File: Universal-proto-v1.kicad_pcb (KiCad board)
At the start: 2 copper layers, 2 parts, among them J1 Bus_ISA_8bit, U1 RP2350B

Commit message: Start work on PCB
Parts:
- added J2: ISA Breakout, Connector_PinHeader_2.54mm:PinHeader_2x31_P2.54mm_Vertical, F.Cu at (185.8, 127.5)
- added J3: Pico GPIO Breakout, Connector_PinHeader_2.54mm:PinHeader_2x25_P2.54mm_Vertical, F.Cu at (180.5, 75.0)
- added JP1: SolderJumper_2_Bridged, Jumper:SolderJumper-2_P1.3mm_Bridged_RoundedPad1.0x1.5mm, F.Cu at (109.5, 122.0)
- added JP10: SolderJumper_2_Bridged, Jumper:SolderJumper-2_P1.3mm_Bridged_RoundedPad1.0x1.5mm, F.Cu at (132.4, 122.0)
- added JP11: SolderJumper_2_Bridged, Jumper:SolderJumper-2_P1.3mm_Bridged_RoundedPad1.0x1.5mm, F.Cu at (134.9, 122.0)
- added JP12: SolderJumper_2_Bridged, Jumper:SolderJumper-2_P1.3mm_Bridged_RoundedPad1.0x1.5mm, F.Cu at (137.5, 122.0)
- added JP13: SolderJumper_2_Bridged, Jumper:SolderJumper-2_P1.3mm_Bridged_RoundedPad1.0x1.5mm, F.Cu at (140.0, 122.0)
- added JP14: SolderJumper_2_Bridged, Jumper:SolderJumper-2_P1.3mm_Bridged_RoundedPad1.0x1.5mm, F.Cu at (142.6, 122.0)
- added JP15: SolderJumper_2_Bridged, Jumper:SolderJumper-2_P1.3mm_Bridged_RoundedPad1.0x1.5mm, F.Cu at (145.1, 122.0)
- added JP16: SolderJumper_2_Bridged, Jumper:SolderJumper-2_P1.3mm_Bridged_RoundedPad1.0x1.5mm, F.Cu at (147.6, 122.0)
- added JP17: SolderJumper_2_Bridged, Jumper:SolderJumper-2_P1.3mm_Bridged_RoundedPad1.0x1.5mm, F.Cu at (150.2, 122.0)
- added JP18: SolderJumper_2_Bridged, Jumper:SolderJumper-2_P1.3mm_Bridged_RoundedPad1.0x1.5mm, F.Cu at (152.7, 122.0)
- added JP19: SolderJumper_2_Bridged, Jumper:SolderJumper-2_P1.3mm_Bridged_RoundedPad1.0x1.5mm, F.Cu at (155.3, 122.0)
- added JP2: SolderJumper_2_Bridged, Jumper:SolderJumper-2_P1.3mm_Bridged_RoundedPad1.0x1.5mm, F.Cu at (112.0, 122.0)
- added JP20: SolderJumper_2_Bridged, Jumper:SolderJumper-2_P1.3mm_Bridged_RoundedPad1.0x1.5mm, F.Cu at (157.8, 122.0)
- added JP21: SolderJumper_2_Bridged, Jumper:SolderJumper-2_P1.3mm_Bridged_RoundedPad1.0x1.5mm, F.Cu at (165.4, 122.0)
- added JP22: SolderJumper_2_Bridged, Jumper:SolderJumper-2_P1.3mm_Bridged_RoundedPad1.0x1.5mm, F.Cu at (168.0, 122.0)
- added JP23: SolderJumper_2_Bridged, Jumper:SolderJumper-2_P1.3mm_Bridged_RoundedPad1.0x1.5mm, F.Cu at (170.5, 122.0)
- added JP24: SolderJumper_2_Bridged, Jumper:SolderJumper-2_P1.3mm_Bridged_RoundedPad1.0x1.5mm, F.Cu at (173.1, 122.0)
- added JP25: SolderJumper_2_Bridged, Jumper:SolderJumper-2_P1.3mm_Bridged_RoundedPad1.0x1.5mm, F.Cu at (175.6, 122.0)
- added JP26: SolderJumper_2_Bridged, Jumper:SolderJumper-2_P1.3mm_Bridged_RoundedPad1.0x1.5mm, F.Cu at (178.1, 122.0)
- added JP27: SolderJumper_2_Bridged, Jumper:SolderJumper-2_P1.3mm_Bridged_RoundedPad1.0x1.5mm, F.Cu at (180.7, 122.0)
- added JP28: SolderJumper_2_Bridged, Jumper:SolderJumper-2_P1.3mm_Bridged_RoundedPad1.0x1.5mm, F.Cu at (183.2, 122.0)
- added JP29: SolderJumper_2_Bridged, Jumper:SolderJumper-2_P1.3mm_Bridged_RoundedPad1.0x1.5mm, B.Cu at (157.8, 122.0)
- added JP3: SolderJumper_2_Bridged, Jumper:SolderJumper-2_P1.3mm_Bridged_RoundedPad1.0x1.5mm, F.Cu at (114.6, 122.0)
- added JP30: SolderJumper_2_Bridged, Jumper:SolderJumper-2_P1.3mm_Bridged_RoundedPad1.0x1.5mm, B.Cu at (160.4, 122.0)
- added JP31: SolderJumper_2_Bridged, Jumper:SolderJumper-2_P1.3mm_Bridged_RoundedPad1.0x1.5mm, B.Cu at (152.7, 122.0)
- added JP32: SolderJumper_2_Bridged, Jumper:SolderJumper-2_P1.3mm_Bridged_RoundedPad1.0x1.5mm, B.Cu at (155.3, 122.0)
- added JP33: SolderJumper_2_Bridged, Jumper:SolderJumper-2_P1.3mm_Bridged_RoundedPad1.0x1.5mm, F.Cu at (160.4, 122.0)
- added JP34: SolderJumper_2_Bridged, Jumper:SolderJumper-2_P1.3mm_Bridged_RoundedPad1.0x1.5mm, B.Cu at (137.5, 122.0)
- added JP35: SolderJumper_2_Bridged, Jumper:SolderJumper-2_P1.3mm_Bridged_RoundedPad1.0x1.5mm, B.Cu at (117.2, 122.0)
- added JP36: SolderJumper_2_Bridged, Jumper:SolderJumper-2_P1.3mm_Bridged_RoundedPad1.0x1.5mm, B.Cu at (183.2, 122.0)
- added JP37: SolderJumper_2_Open, Jumper:SolderJumper-2_P1.3mm_Open_Pad1.0x1.5mm, B.Cu at (165.5, 133.8)
- added JP38: SolderJumper_2_Open, Jumper:SolderJumper-2_P1.3mm_Open_Pad1.0x1.5mm, B.Cu at (170.6, 133.8)
- added JP39: SolderJumper_2_Open, Jumper:SolderJumper-2_P1.3mm_Open_Pad1.0x1.5mm, B.Cu at (175.7, 133.8)
- added JP4: SolderJumper_2_Bridged, Jumper:SolderJumper-2_P1.3mm_Bridged_RoundedPad1.0x1.5mm, F.Cu at (117.1, 122.0)
- added JP5: SolderJumper_2_Bridged, Jumper:SolderJumper-2_P1.3mm_Bridged_RoundedPad1.0x1.5mm, F.Cu at (119.7, 122.0)
- added JP6: SolderJumper_2_Bridged, Jumper:SolderJumper-2_P1.3mm_Bridged_RoundedPad1.0x1.5mm, F.Cu at (122.2, 122.0)
- added JP7: SolderJumper_2_Bridged, Jumper:SolderJumper-2_P1.3mm_Bridged_RoundedPad1.0x1.5mm, F.Cu at (124.8, 122.0)
- added JP8: SolderJumper_2_Bridged, Jumper:SolderJumper-2_P1.3mm_Bridged_RoundedPad1.0x1.5mm, F.Cu at (127.3, 122.0)
- added JP9: SolderJumper_2_Bridged, Jumper:SolderJumper-2_P1.3mm_Bridged_RoundedPad1.0x1.5mm, F.Cu at (129.8, 122.0)
- added U2: ~, FujiNet:ESP32-S3-CAM, F.Cu at (183.5, 40.8)
- U1: value RP2350B -> ~; footprint Package_DFN_QFN:QFN-80-1EP_10x10mm_P0.4mm_EP3.4x3.4mm -> FujiNet:WaveShare-Core-RP2350B
- moved J1 78.6 mm to (185.9, 140.0)
- moved U1 35.5 mm to (90.9, 71.9)
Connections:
- J1 pad 1: unconnected-(J1-GND-Pad1) -> /GND
- J1 pad 10: unconnected-(J1-GND-Pad10) -> /GND
- J1 pad 11: unconnected-(J1-~{SMEMW}-Pad11) -> /~{SMEMW}
- J1 pad 12: unconnected-(J1-~{SMEMR}-Pad12) -> /~{SMEMR}
- J1 pad 13: unconnected-(J1-~{IOW}-Pad13) -> /~{IOW}
- J1 pad 14: unconnected-(J1-~{IOR}-Pad14) -> /~{IOR}
- J1 pad 15: unconnected-(J1-~{DACK3}-Pad15) -> /~{DACK3}
- J1 pad 16: unconnected-(J1-DRQ3-Pad16) -> /DRQ3
- J1 pad 17: unconnected-(J1-~{DACK1}-Pad17) -> /~{DACK1}
- J1 pad 18: unconnected-(J1-DRQ1-Pad18) -> /DRQ1
- J1 pad 19: unconnected-(J1-~{DACK0}-Pad19) -> /~{DACK0}
- J1 pad 2: unconnected-(J1-RESET-Pad2) -> /RESET
- J1 pad 20: unconnected-(J1-CLK-Pad20) -> /CLK
- J1 pad 21: unconnected-(J1-IRQ7-Pad21) -> /IRQ7
- J1 pad 22: unconnected-(J1-IRQ6-Pad22) -> /IRQ6
- J1 pad 23: unconnected-(J1-IRQ5-Pad23) -> /IRQ5
- J1 pad 24: unconnected-(J1-IRQ4-Pad24) -> /IRQ4
- J1 pad 25: unconnected-(J1-IRQ3-Pad25) -> /IRQ3
- J1 pad 26: unconnected-(J1-~{DACK2}-Pad26) -> /~{DACK2}
- J1 pad 27: unconnected-(J1-TC-Pad27) -> /TC
- J1 pad 28: unconnected-(J1-ALE-Pad28) -> /ALE
- J1 pad 29: unconnected-(J1-VCC-Pad29) -> /VCC
- J1 pad 3: unconnected-(J1-VCC-Pad3) -> /VCC
- J1 pad 30: unconnected-(J1-OSC-Pad30) -> /OSC
- J1 pad 31: unconnected-(J1-GND-Pad31) -> /GND
- J1 pad 32: unconnected-(J1-IO-Pad32) -> /IO
- J1 pad 33: unconnected-(J1-DB7-Pad33) -> /DB7
- J1 pad 34: unconnected-(J1-DB6-Pad34) -> /DB6
- J1 pad 35: unconnected-(J1-DB5-Pad35) -> /DB5
- J1 pad 36: unconnected-(J1-DB4-Pad36) -> /DB4
- J1 pad 37: unconnected-(J1-DB3-Pad37) -> /DB3
- J1 pad 38: unconnected-(J1-DB2-Pad38) -> /DB2
- J1 pad 39: unconnected-(J1-DB1-Pad39) -> /DB1
- J1 pad 4: unconnected-(J1-IRQ2-Pad4) -> /IRQ2
- J1 pad 40: unconnected-(J1-DB0-Pad40) -> /DB0
- J1 pad 41: unconnected-(J1-IO_READY-Pad41) -> /IO_READY
- J1 pad 42: unconnected-(J1-AEN-Pad42) -> /AEN
- J1 pad 43: unconnected-(J1-BA19-Pad43) -> /BA19
- J1 pad 44: unconnected-(J1-BA18-Pad44) -> /BA18
- J1 pad 45: unconnected-(J1-BA17-Pad45) -> /BA17
- J1 pad 46: unconnected-(J1-BA16-Pad46) -> /BA16
- J1 pad 47: unconnected-(J1-BA15-Pad47) -> /BA15
- J1 pad 48: unconnected-(J1-BA14-Pad48) -> /BA14
- J1 pad 49: unconnected-(J1-BA13-Pad49) -> /BA13
- J1 pad 5: unconnected-(J1--5V-Pad5) -> /ISA_-5V
- J1 pad 50: unconnected-(J1-BA12-Pad50) -> /BA12
- J1 pad 51: unconnected-(J1-BA11-Pad51) -> /BA11
- J1 pad 52: unconnected-(J1-BA10-Pad52) -> /BA10
- J1 pad 53: unconnected-(J1-BA09-Pad53) -> /BA09
- J1 pad 54: unconnected-(J1-BA08-Pad54) -> /BA08
- J1 pad 55: unconnected-(J1-BA07-Pad55) -> /BA07
- J1 pad 56: unconnected-(J1-BA06-Pad56) -> /BA06
- J1 pad 57: unconnected-(J1-BA05-Pad57) -> /BA05
- J1 pad 58: unconnected-(J1-BA04-Pad58) -> /BA04
- J1 pad 59: unconnected-(J1-BA03-Pad59) -> /BA03
- J1 pad 6: unconnected-(J1-DRQ2-Pad6) -> /DRQ2
- J1 pad 60: unconnected-(J1-BA02-Pad60) -> /BA02
- J1 pad 61: unconnected-(J1-BA01-Pad61) -> /BA01
- J1 pad 62: unconnected-(J1-BA00-Pad62) -> /BA00
- J1 pad 7: unconnected-(J1--12V-Pad7) -> /ISA_-12V
- J1 pad 8: unconnected-(J1-UNUSED-Pad8) -> /UNUSED
- J1 pad 9: unconnected-(J1-+12V-Pad9) -> /ISA_+12V
- U1 pad 1: unconnected-(U1-GPIO4-Pad1) -> /GP1_ISA_A1
- U1 pad 10: Net-(U1-DVDD-Pad10) -> /GP10_ISA_A10
- U1 pad 11: unconnected-(U1-GPIO12-Pad11) -> /GP11_ISA_A11
- U1 pad 12: unconnected-(U1-GPIO13-Pad12) -> /GP12_ISA_A12
- U1 pad 13: unconnected-(U1-GPIO14-Pad13) -> /GP13_ISA_A13
- U1 pad 14: unconnected-(U1-GPIO15-Pad14) -> /GP14_ISA_A14
- U1 pad 15: Net-(U1-IOVDD-Pad15) -> /GP15_ISA_A15
- U1 pad 16: unconnected-(U1-GPIO16-Pad16) -> /GP16_ISA_A16
- U1 pad 17: unconnected-(U1-GPIO17-Pad17) -> /GP17_ISA_A17
- U1 pad 18: unconnected-(U1-GPIO18-Pad18) -> /GP18_ISA_A18
- U1 pad 19: unconnected-(U1-GPIO19-Pad19) -> /GP19_ISA_A19
- U1 pad 2: unconnected-(U1-GPIO5-Pad2) -> /GP2_ISA_A2
- U1 pad 20: unconnected-(U1-GPIO20-Pad20) -> /GP20_ISA_D0
- U1 pad 21: unconnected-(U1-GPIO21-Pad21) -> /GP21_ISA_D1
- U1 pad 22: unconnected-(U1-GPIO22-Pad22) -> /GP22_ISA_D2
- U1 pad 23: unconnected-(U1-GPIO23-Pad23) -> /GP23_ISA_D3
- U1 pad 24: Net-(U1-IOVDD-Pad15) -> /GP24_ISA_D4
- U1 pad 25: unconnected-(U1-GPIO24-Pad25) -> /GP25_ISA_D5
- U1 pad 26: unconnected-(U1-GPIO25-Pad26) -> /GP26_ISA_D6
- U1 pad 27: unconnected-(U1-GPIO26-Pad27) -> /GP27_ISA_D7
- U1 pad 28: unconnected-(U1-GPIO27-Pad28) -> /GP28_ISA_MEMR
- U1 pad 29: Net-(U1-IOVDD-Pad15) -> /GP29_ISA_MEMW
- U1 pad 3: unconnected-(U1-GPIO6-Pad3) -> /GP3_ISA_A3
- U1 pad 30: unconnected-(U1-XIN-Pad30) -> /GP30_ISA_IOR
- U1 pad 31: unconnected-(U1-XOUT-Pad31) -> /GP31_ISA_IOW
- U1 pad 32: Net-(U1-DVDD-Pad10) -> /GP32_ISA_AEN
- U1 pad 33: unconnected-(U1-SWCLK-Pad33) -> /GP33_ISA_CLK
- U1 pad 34: unconnected-(U1-SWDIO-Pad34) -> /GP34_ISA_ALE
- U1 pad 35: unconnected-(U1-RUN-Pad35) -> /GP35_ISA_RESET
- U1 pad 36: unconnected-(U1-GPIO28-Pad36) -> /GP36
- U1 pad 37: unconnected-(U1-GPIO29-Pad37) -> /GP37
- U1 pad 38: unconnected-(U1-GPIO30-Pad38) -> /GP38
- U1 pad 39: unconnected-(U1-GPIO31-Pad39) -> /GP39
- U1 pad 4: unconnected-(U1-GPIO7-Pad4) -> /GP4_ISA_A4
- U1 pad 40: unconnected-(U1-GPIO32-Pad40) -> /GP40
- U1 pad 41: Net-(U1-IOVDD-Pad15) -> /GP41
- U1 pad 42: unconnected-(U1-GPIO33-Pad42) -> /GP42
- U1 pad 43: unconnected-(U1-GPIO34-Pad43) -> /GP43
- U1 pad 44: unconnected-(U1-GPIO35-Pad44) -> /GP44
- U1 pad 45: unconnected-(U1-GPIO36-Pad45) -> /GP45
- U1 pad 46: unconnected-(U1-GPIO37-Pad46) -> /GP46
- U1 pad 47: unconnected-(U1-GPIO38-Pad47) -> /GP47
- U1 pad 5: Net-(U1-IOVDD-Pad15) -> /GP5_ISA_A5
- U1 pad 6: unconnected-(U1-GPIO8-Pad6) -> /GP6_ISA_A6
- U1 pad 7: unconnected-(U1-GPIO9-Pad7) -> /GP7_ISA_A7
- U1 pad 8: unconnected-(U1-GPIO10-Pad8) -> /GP8_ISA_A8
- U1 pad 9: unconnected-(U1-GPIO11-Pad9) -> /GP9_ISA_A9
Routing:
- net /GND: track 0.00 -> 40.2 mm
- net /VCC: track 0.00 -> 26.8 mm
- net /UNUSED: track 0.00 -> 13.6 mm
- net /~{IOR}: track 0.00 -> 13.5 mm
- net /~{SMEMR}: track 0.00 -> 13.4 mm
- net /~{IOW}: track 0.00 -> 13.4 mm
- net /~{DACK0}: track 0.00 -> 13.4 mm
- net /RESET: track 0.00 -> 13.4 mm
- net /IRQ5: track 0.00 -> 13.4 mm
- net /IRQ4: track 0.00 -> 13.4 mm
- net /DRQ3: track 0.00 -> 13.4 mm
- net /DRQ2: track 0.00 -> 13.4 mm
- net /CLK: track 0.00 -> 13.4 mm
- net /OSC: track 0.00 -> 13.4 mm
- net /~{DACK3}: track 0.00 -> 13.4 mm
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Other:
- board outline added: 81.5 x 94 mm

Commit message: Connect ISA pins to solder jumpers
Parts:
- moved U1 73.6 mm to (162.4, 89.4)
- moved J3 8.04 mm to (180.5, 67.0)
- moved U2 8.04 mm to (183.5, 32.8)
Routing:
- net /DB0: track 10.0 -> 18.5 mm
- net /BA00: track 10.0 -> 18.4 mm
- net /BA01: track 10.0 -> 18.4 mm
- net /BA02: track 10.0 -> 18.4 mm
- net /BA03: track 10.0 -> 18.4 mm
- net /BA04: track 10.0 -> 18.4 mm
- net /BA05: track 10.0 -> 18.4 mm
- net /BA06: track 10.0 -> 18.4 mm
- net /BA07: track 10.0 -> 18.4 mm
- net /BA08: track 10.0 -> 18.4 mm
- net /BA09: track 10.0 -> 18.4 mm
- net /BA10: track 10.0 -> 18.4 mm
- net /BA11: track 10.0 -> 18.4 mm
- net /BA12: track 10.0 -> 18.4 mm
- net /BA13: track 10.0 -> 18.4 mm
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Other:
- board size 81.5 x 94 mm -> 81.5 x 107.5 mm

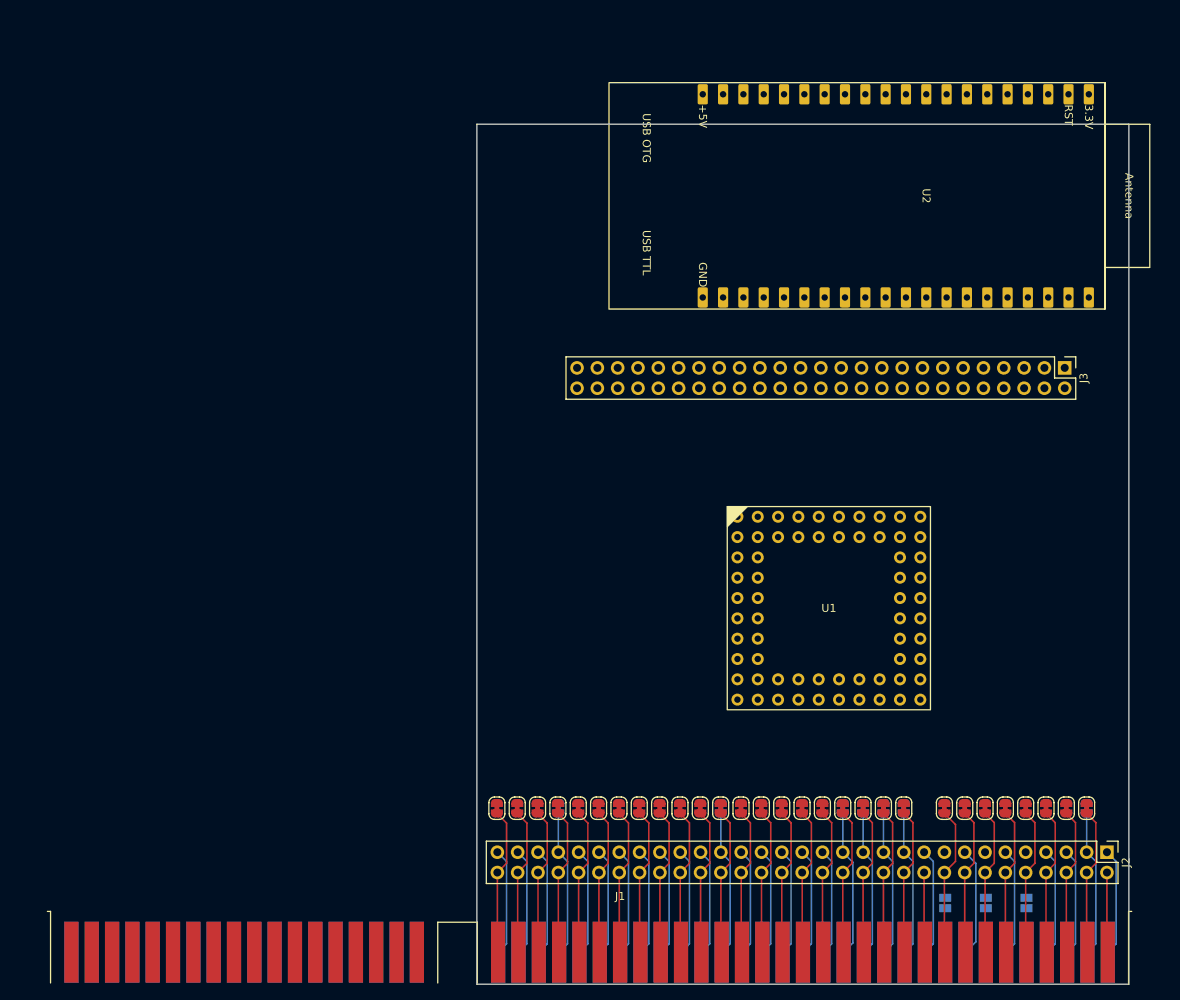
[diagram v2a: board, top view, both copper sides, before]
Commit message: zig-zag around GPIO breakout, ISA connected to Core2350
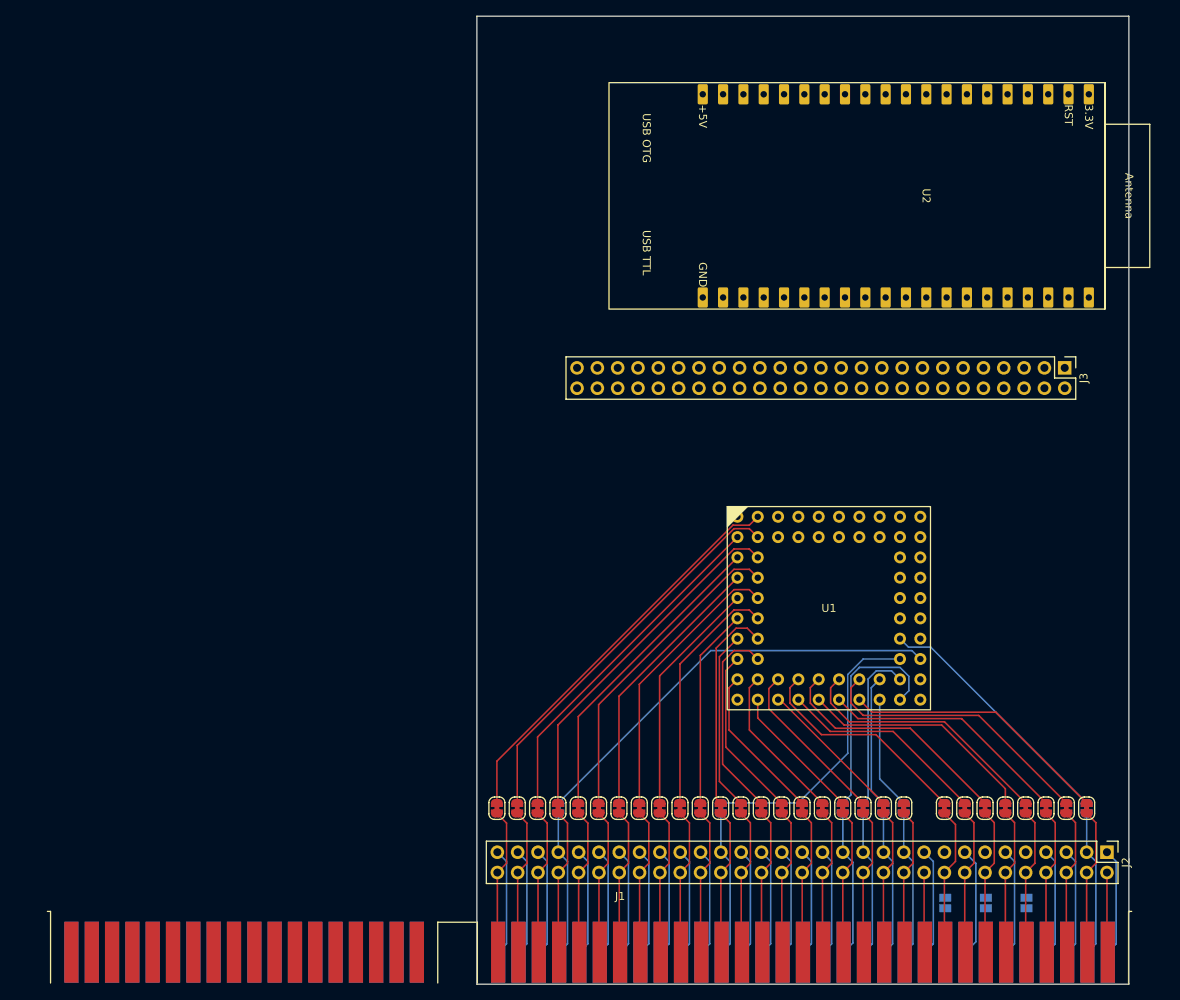
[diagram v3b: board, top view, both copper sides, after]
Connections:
- J3 pad 10: /GP44 -> /GP7_ISA_A7
- J3 pad 11: /GP5_ISA_A5 -> /GP10_ISA_A10
- J3 pad 12: /GP43 -> /GP9_ISA_A9
- J3 pad 13: /GP6_ISA_A6 -> /GP12_ISA_A12
- J3 pad 14: /GP42 -> /GP11_ISA_A11
- J3 pad 15: /GP7_ISA_A7 -> /GP14_ISA_A14
- J3 pad 16: /GP41 -> /GP13_ISA_A13
- J3 pad 17: /GP8_ISA_A8 -> /GP16_ISA_A16
- J3 pad 18: /GP40 -> /GP15_ISA_A15
- J3 pad 19: /GP9_ISA_A9 -> /GP18_ISA_A18
- J3 pad 20: /GP39 -> /GP17_ISA_A17
- J3 pad 21: /GP10_ISA_A10 -> /GP20_ISA_D0
- J3 pad 22: /GP38 -> /GP19_ISA_A19
- J3 pad 23: /GP11_ISA_A11 -> /GP22_ISA_D2
- J3 pad 24: /GP37 -> /GP21_ISA_D1
- J3 pad 25: /GP12_ISA_A12 -> /GP24_ISA_D4
- J3 pad 26: /GP36 -> /GP23_ISA_D3
- J3 pad 27: /GP13_ISA_A13 -> /GP26_ISA_D6
- J3 pad 28: /GP35_ISA_RESET -> /GP25_ISA_D5
- J3 pad 29: /GP14_ISA_A14 -> /GP28_ISA_MEMR
- J3 pad 3: /GP1_ISA_A1 -> /GP2_ISA_A2
- J3 pad 30: /GP34_ISA_ALE -> /GP27_ISA_D7
- J3 pad 31: /GP15_ISA_A15 -> /GP30_ISA_IOR
- J3 pad 32: /GP33_ISA_CLK -> /GP29_ISA_MEMW
- J3 pad 33: /GP16_ISA_A16 -> /GP32_ISA_AEN
- J3 pad 34: /GP32_ISA_AEN -> /GP31_ISA_IOW
- J3 pad 35: /GP17_ISA_A17 -> /GP34_ISA_ALE
- J3 pad 36: /GP31_ISA_IOW -> /GP33_ISA_CLK
- J3 pad 37: /GP18_ISA_A18 -> /GP36
- J3 pad 38: /GP30_ISA_IOR -> /GP35_ISA_RESET
- J3 pad 39: /GP19_ISA_A19 -> /GP38
- J3 pad 4: /GP47 -> /GP1_ISA_A1
- J3 pad 40: /GP29_ISA_MEMW -> /GP37
- J3 pad 41: /GP20_ISA_D0 -> /GP40
- J3 pad 42: /GP28_ISA_MEMR -> /GP39
- J3 pad 43: /GP21_ISA_D1 -> /GP42
- J3 pad 44: /GP27_ISA_D7 -> /GP41
- J3 pad 45: /GP22_ISA_D2 -> /GP44
- J3 pad 46: /GP26_ISA_D6 -> /GP43
- J3 pad 47: /GP23_ISA_D3 -> /GP46
- J3 pad 48: /GP25_ISA_D5 -> /GP45
- J3 pad 5: /GP2_ISA_A2 -> /GP4_ISA_A4
- J3 pad 50: /GP24_ISA_D4 -> /GP47
- J3 pad 6: /GP46 -> /GP3_ISA_A3
- J3 pad 7: /GP3_ISA_A3 -> /GP6_ISA_A6
- J3 pad 8: /GP45 -> /GP5_ISA_A5
- J3 pad 9: /GP4_ISA_A4 -> /GP8_ISA_A8
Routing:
- net /GP34_ISA_ALE: track 0.00 -> 53.6 mm
- net /GP0_ISA_A0: track 0.00 -> 50.5 mm
- net /GP1_ISA_A1: track 0.00 -> 48.9 mm
- net /GP3_ISA_A3: track 0.00 -> 44.3 mm
- net /GP2_ISA_A2: track 0.00 -> 43.6 mm
- net /GP5_ISA_A5: track 0.00 -> 39.6 mm
- net /GP4_ISA_A4: track 0.00 -> 38.9 mm
- net /GP33_ISA_CLK: track 0.00 -> 35.6 mm
- net /GP26_ISA_D6: track 0.00 -> 35.5 mm
- net /GP7_ISA_A7: track 0.00 -> 35.0 mm
- net /GP6_ISA_A6: track 0.00 -> 34.3 mm
- net /GP27_ISA_D7: track 0.00 -> 33.8 mm
- net /GP24_ISA_D4: track 0.00 -> 33.0 mm
- net /GP35_ISA_RESET: track 0.00 -> 31.8 mm
- net /GP25_ISA_D5: track 0.00 -> 31.2 mm
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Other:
- board size 81.5 x 107.5 mm -> 81.5 x 121 mm

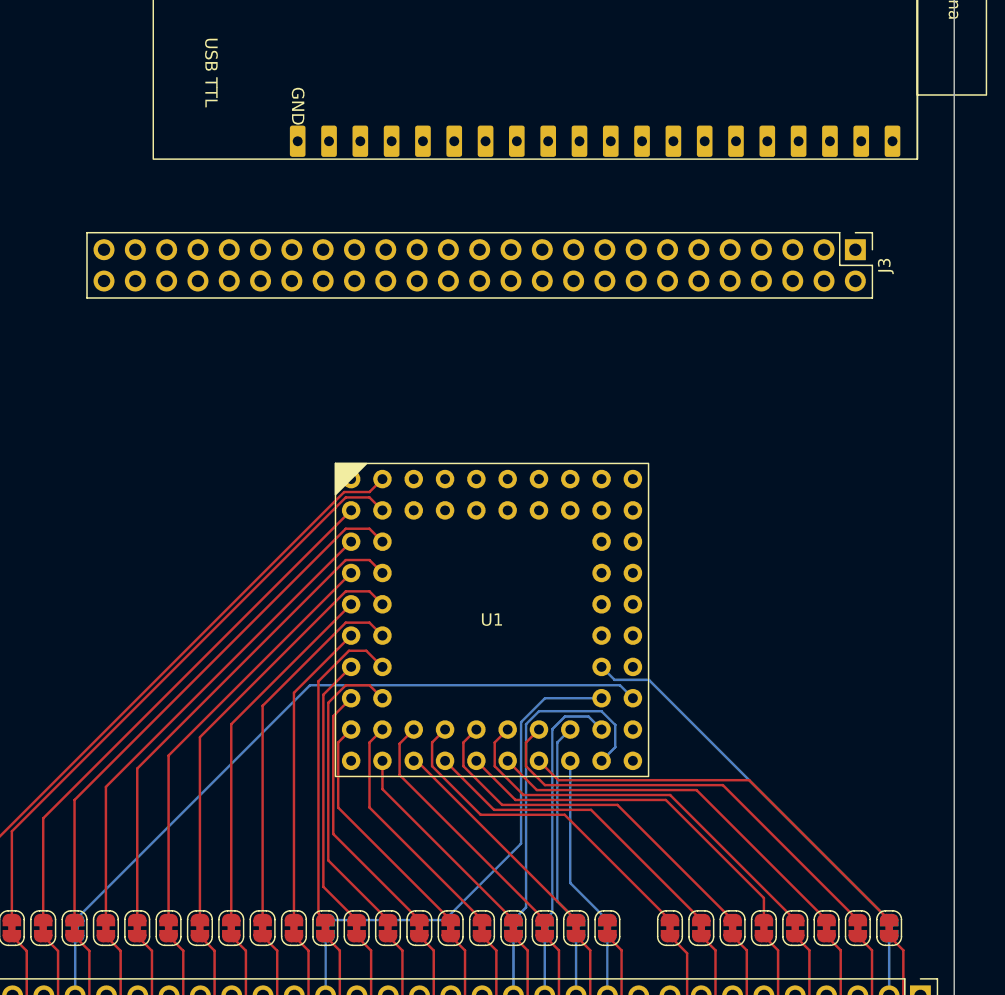
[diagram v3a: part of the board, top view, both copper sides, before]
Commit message: GPIO breakout is routed
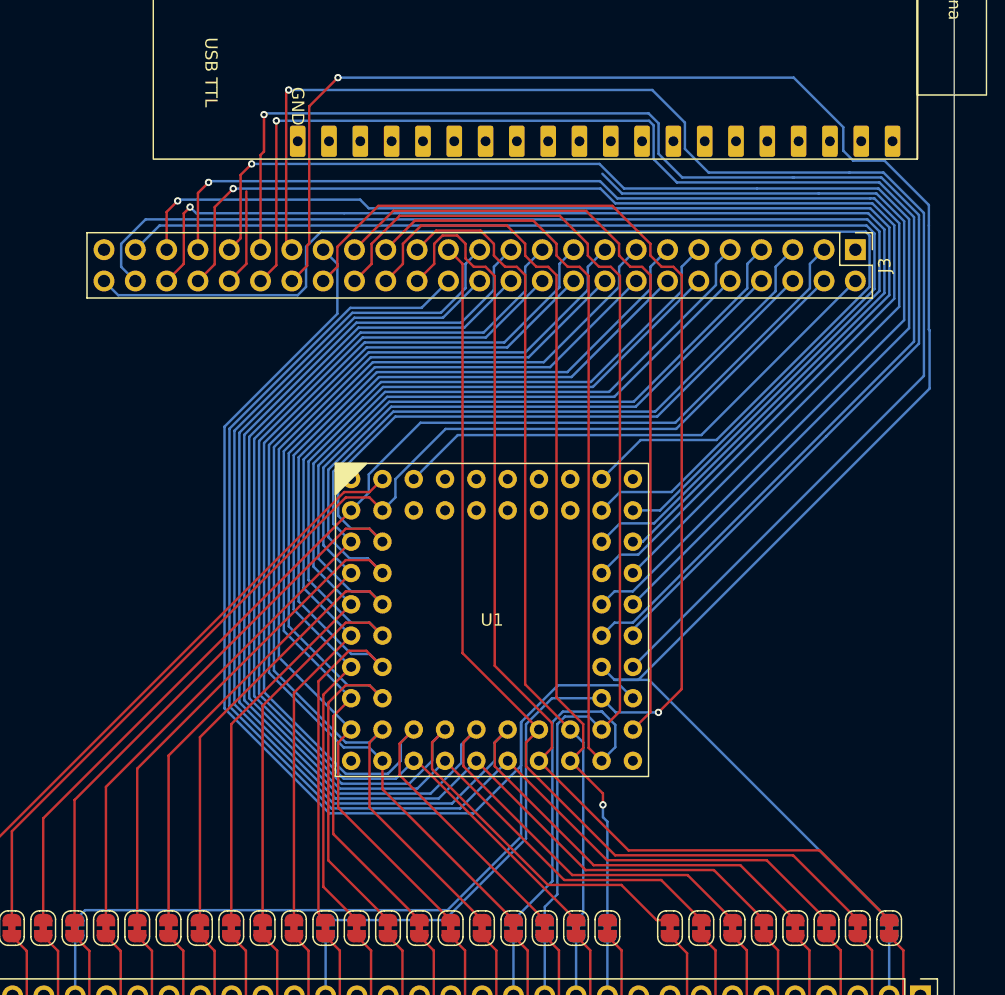
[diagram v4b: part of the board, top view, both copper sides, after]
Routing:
- net /GP35_ISA_RESET: track 31.8 -> 153.5 mm, vias 0 -> 1
- net /GP36: track 0.00 -> 116.8 mm, vias 0 -> 1
- net /GP37: track 0.00 -> 115.4 mm, vias 0 -> 1
- net /GP38: track 0.00 -> 113.0 mm, vias 0 -> 1
- net /GP40: track 0.00 -> 103.4 mm, vias 0 -> 1
- net /GP41: track 0.00 -> 102.5 mm, vias 0 -> 1
- net /GP42: track 0.00 -> 100.6 mm, vias 0 -> 1
- net /GP43: track 0.00 -> 100.3 mm, vias 0 -> 1
- net /GP47: track 0.00 -> 99.1 mm
- net /GP45: track 0.00 -> 98.5 mm
- net /GP44: track 0.00 -> 97.6 mm, vias 0 -> 1
- net /GP46: track 0.00 -> 95.1 mm
- net /GP34_ISA_ALE: track 53.6 -> 133.2 mm
- net /GP24_ISA_D4: track 33.0 -> 111.2 mm
- net /GP33_ISA_CLK: track 35.6 -> 112.1 mm, vias 0 -> 1
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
